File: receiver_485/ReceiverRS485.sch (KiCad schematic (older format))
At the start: 25 parts, among them U25 USB3_duplo, U26 USB3_duplo

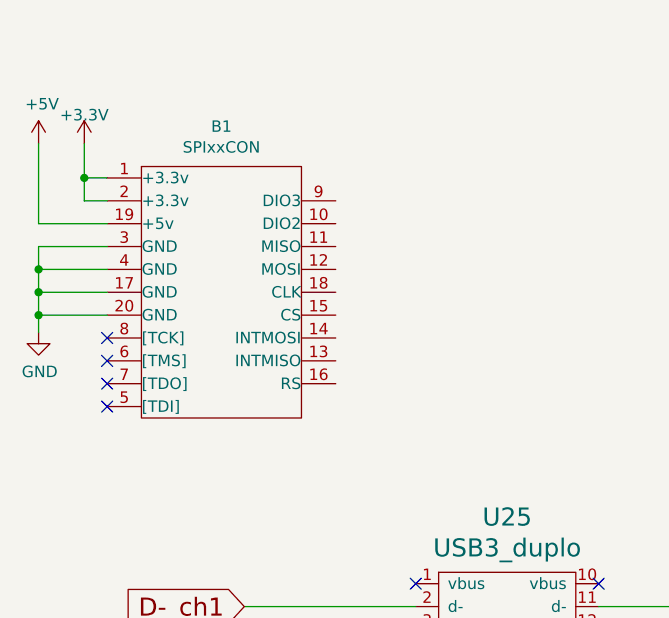
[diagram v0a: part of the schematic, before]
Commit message: Changed version of SPIxxcCON BUS
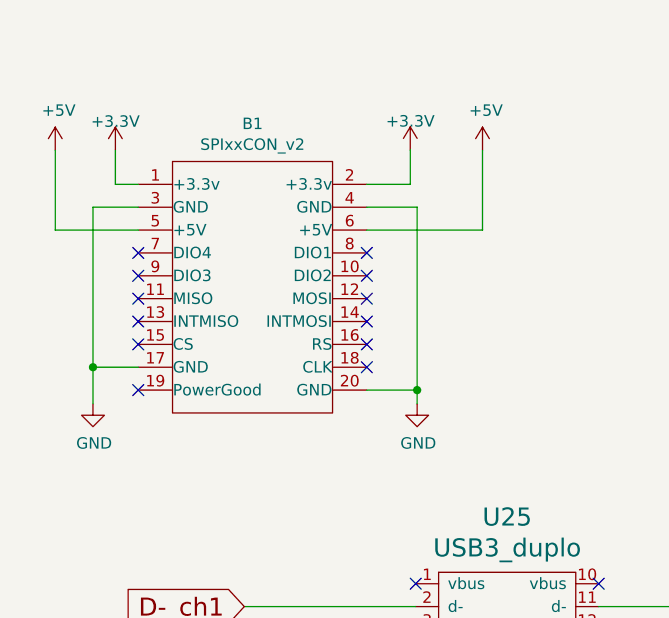
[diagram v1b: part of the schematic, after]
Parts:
- removed B1: SPIxxCON, Connector_PinHeader_2.54mm:PinHeader_2x10_P2.54mm_Vertical, symbol ReceiverRS485-rescue:SPIxxCON-Controle
- added B1: SPIxxCON_v2, Controle:SPIxxCON_(only_connector), symbol Controle:SPIxxCON_v2
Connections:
- net +3V3: now also B1.1 (+3.3v), B1.2 (+3.3v)
- net +5V: now also B1.5 (+5V), B1.6 (+5V)
- net GND: now also B1.17 (GND), B1.20 (GND), B1.3 (GND), B1.4 (GND)
- no-connect marks 24 -> 32
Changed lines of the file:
@@
 EESchema Schematic File Version 4
-LIBS:ReceiverRS485-cache
-EELAYER 26 0
+EELAYER 30 0
 EELAYER END
 $Descr A4 11693 8268
@@
 Comment4 ""
 $EndDescr
-$Comp
-L ReceiverRS485-rescue:SPIxxCON-Controle B1
-U 1 1 6047D9C8
-P 2100 1725
-F 0 "B1" H 2100 2450 50  0000 C CNN
-F 1 "SPIxxCON" H 2100 2359 50  0000 C CNN
-F 2 "Connector_PinHeader_2.54mm:PinHeader_2x10_P2.54mm_Vertical" H 2100 525 60  0001 C CNN
-F 3 "" H 2100 525 60  0000 C CNN
-	1    2100 1725
-	1    0    0    -1
-$EndComp
-NoConn ~ 1600 1925
-NoConn ~ 1600 2025
-NoConn ~ 1600 2125
-NoConn ~ 1600 2225
-$Comp
-L power:GND #PWR0101
-U 1 1 60487043
-P 1300 1900
-F 0 "#PWR0101" H 1300 1650 50  0001 C CNN
-F 1 "GND" H 1305 1727 50  0000 C CNN
-F 2 "" H 1300 1900 50  0001 C CNN
-F 3 "" H 1300 1900 50  0001 C CNN
-	1    1300 1900
-	1    0    0    -1
-$EndComp
-Wire Wire Line
-	1300 1900 1300 1825
-Wire Wire Line
-	1300 1825 1600 1825
-Wire Wire Line
-	1600 1725 1300 1725
-Wire Wire Line
-	1300 1725 1300 1825
-Connection ~ 1300 1825
-Wire Wire Line
-	1600 1625 1300 1625
-Wire Wire Line
-	1300 1625 1300 1725
-Connection ~ 1300 1725
-Wire Wire Line
-	1600 1525 1300 1525
-Wire Wire Line
-	1300 1525 1300 1625
-Connection ~ 1300 1625
-Wire Wire Line
-	1600 1325 1500 1325
-Wire Wire Line
-	1500 1325 1500 1225
-Wire Wire Line
-	1600 1225 1500 1225
-Connection ~ 1500 1225
-Wire Wire Line
-	1500 1225 1500 1075
-Wire Wire Line
-	1600 1425 1300 1425
-Wire Wire Line
-	1300 1425 1300 1075
+Wire Wire Line
+	1736 1253 1636 1253
+Wire Wire Line
+	1636 1253 1636 1103
+Wire Wire Line
+	1373 1453 1373 1103
 $Comp
 L power:+5V #PWR0102
 U 1 1 6048CC18
-P 1300 1075
-F 0 "#PWR0102" H 1300 925 50  0001 C CNN
-F 1 "+5V" H 1315 1248 50  0000 C CNN
-F 2 "" H 1300 1075 50  0001 C CNN
-F 3 "" H 1300 1075 50  0001 C CNN
-	1    1300 1075
+P 1373 1103
+F 0 "#PWR0102" H 1373 953 50  0001 C CNN
+F 1 "+5V" H 1388 1276 50  0000 C CNN
+F 2 "" H 1373 1103 50  0001 C CNN
+F 3 "" H 1373 1103 50  0001 C CNN
+	1    1373 1103
 	1    0    0    -1
 $EndComp
@@
 L power:+3.3V #PWR0103
 U 1 1 6048D724
-P 1500 1075
-F 0 "#PWR0103" H 1500 925 50  0001 C CNN
-F 1 "+3.3V" H 1500 1200 50  0000 C CNN
-F 2 "" H 1500 1075 50  0001 C CNN
-F 3 "" H 1500 1075 50  0001 C CNN
-	1    1500 1075
+P 1636 1103
+F 0 "#PWR0103" H 1636 953 50  0001 C CNN
+F 1 "+3.3V" H 1636 1228 50  0000 C CNN
+F 2 "" H 1636 1103 50  0001 C CNN
+F 3 "" H 1636 1103 50  0001 C CNN
+	1    1636 1103
 	1    0    0    -1
 $EndComp
@@
 Wire Wire Line
 	4050 6250 4500 6250
+$Comp
+L Controle:SPIxxCON_v2 B1
+U 1 1 60BEB115
+P 2236 1703
+F 0 "B1" H 2236 2418 50  0000 C CNN
+F 1 "SPIxxCON_v2" H 2236 2327 50  0000 C CNN
+F 2 "Controle:SPIxxCON_(only_connector)" H 2236 503 60  0001 C CNN
+F 3 "" H 2236 503 60  0000 C CNN
+	1    2236 1703
+	1    0    0    -1
+$EndComp
+$Comp
+L power:+3.3V #PWR0117
+U 1 1 60BFED9F
+P 2926 1102
+F 0 "#PWR0117" H 2926 952 50  0001 C CNN
+F 1 "+3.3V" H 2926 1227 50  0000 C CNN
+F 2 "" H 2926 1102 50  0001 C CNN
+F 3 "" H 2926 1102 50  0001 C CNN
+	1    2926 1102
+	1    0    0    -1
+$EndComp
+Wire Wire Line
+	2926 1102 2926 1253
+Wire Wire Line
+	2926 1253 2736 1253
+Wire Wire Line
+	1373 1453 1736 1453
+Wire Wire Line
+	3242 1453 3242 1103
+$Comp
+L power:+5V #PWR0124
+U 1 1 60C4564D
+P 3242 1103
+F 0 "#PWR0124" H 3242 953 50  0001 C CNN
+F 1 "+5V" H 3257 1276 50  0000 C CNN
+F 2 "" H 3242 1103 50  0001 C CNN
+F 3 "" H 3242 1103 50  0001 C CNN
+	1    3242 1103
+	1    0    0    -1
+$EndComp
+Wire Wire Line
+	2736 1453 3242 1453
+$Comp
+L power:GND #PWR0101
+U 1 1 60487043
+P 1538 2213
+F 0 "#PWR0101" H 1538 1963 50  0001 C CNN
+F 1 "GND" H 1543 2040 50  0000 C CNN
+F 2 "" H 1538 2213 50  0001 C CNN
+F 3 "" H 1538 2213 50  0001 C CNN
+	1    1538 2213
+	1    0    0    -1
+$EndComp
+Wire Wire Line
+	1736 1353 1538 1353
+Wire Wire Line
+	1538 1353 1538 2053
+Wire Wire Line
+	1736 2053 1538 2053
+Connection ~ 1538 2053
+Wire Wire Line
+	1538 2053 1538 2213
+$Comp
+L power:GND #PWR0126
+U 1 1 60C95FA3
+P 2956 2213
+F 0 "#PWR0126" H 2956 1963 50  0001 C CNN
+F 1 "GND" H 2961 2040 50  0000 C CNN
+F 2 "" H 2956 2213 50  0001 C CNN
+F 3 "" H 2956 2213 50  0001 C CNN
+	1    2956 2213
+	1    0    0    -1
+$EndComp
+Wire Wire Line
+	2736 2153 2956 2153
+Wire Wire Line
+	2956 2153 2956 2213
+Wire Wire Line
+	2956 2153 2956 1353
+Wire Wire Line
+	2956 1353 2736 1353
+Connection ~ 2956 2153
+NoConn ~ 1736 1553
+NoConn ~ 1736 1653
+NoConn ~ 1736 1753
+NoConn ~ 1736 1853
+NoConn ~ 1736 1953
+NoConn ~ 1736 2153
+NoConn ~ 2736 2053
+NoConn ~ 2736 1953
+NoConn ~ 2736 1853
+NoConn ~ 2736 1753
+NoConn ~ 2736 1653
+NoConn ~ 2736 1553
 $EndSCHEMATC

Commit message: update receiver pcb
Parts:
- renumbered U26 to J10, U25 to J9
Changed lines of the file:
@@
 Connection ~ 8050 4000
 $Comp
-L ReceiverRS485-rescue:USB3_duplo-FRDM-KL25Z U25
+L ReceiverRS485-rescue:USB3_duplo-FRDM-KL25Z J9
 U 1 1 6065F4BF
 P 3050 3000
-F 0 "U25" H 3350 3291 79  0000 C CNN
+F 0 "J9" H 3350 3291 79  0000 C CNN
 F 1 "USB3_duplo" H 3350 3156 79  0000 C CNN
 F 2 "kl25_xx:USB3_DUPLO" H 3050 3000 79  0001 C CNN
@@
 $EndComp
 $Comp
-L ReceiverRS485-rescue:USB3_duplo-FRDM-KL25Z U26
+L ReceiverRS485-rescue:USB3_duplo-FRDM-KL25Z J10
 U 1 1 6065F5B3
 P 3050 5100
-F 0 "U26" H 3350 5391 79  0000 C CNN
+F 0 "J10" H 3350 5391 79  0000 C CNN
 F 1 "USB3_duplo" H 3350 5256 79  0000 C CNN
 F 2 "kl25_xx:USB3_DUPLO" H 3050 5100 79  0001 C CNN
